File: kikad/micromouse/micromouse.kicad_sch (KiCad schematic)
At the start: 4 parts

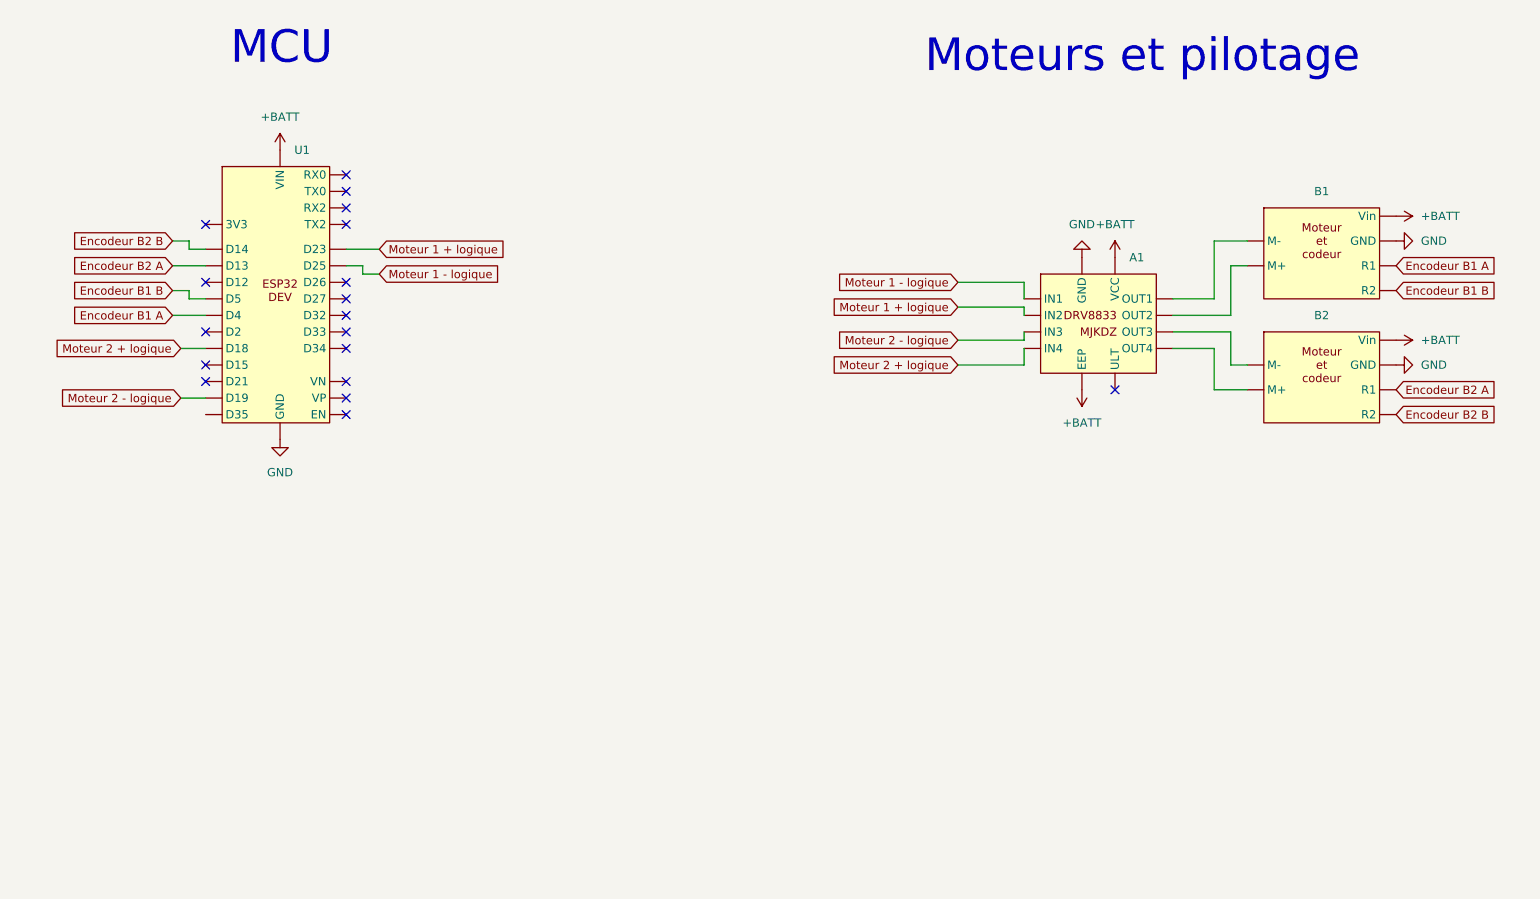
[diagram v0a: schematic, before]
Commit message: Changement micromouse svg
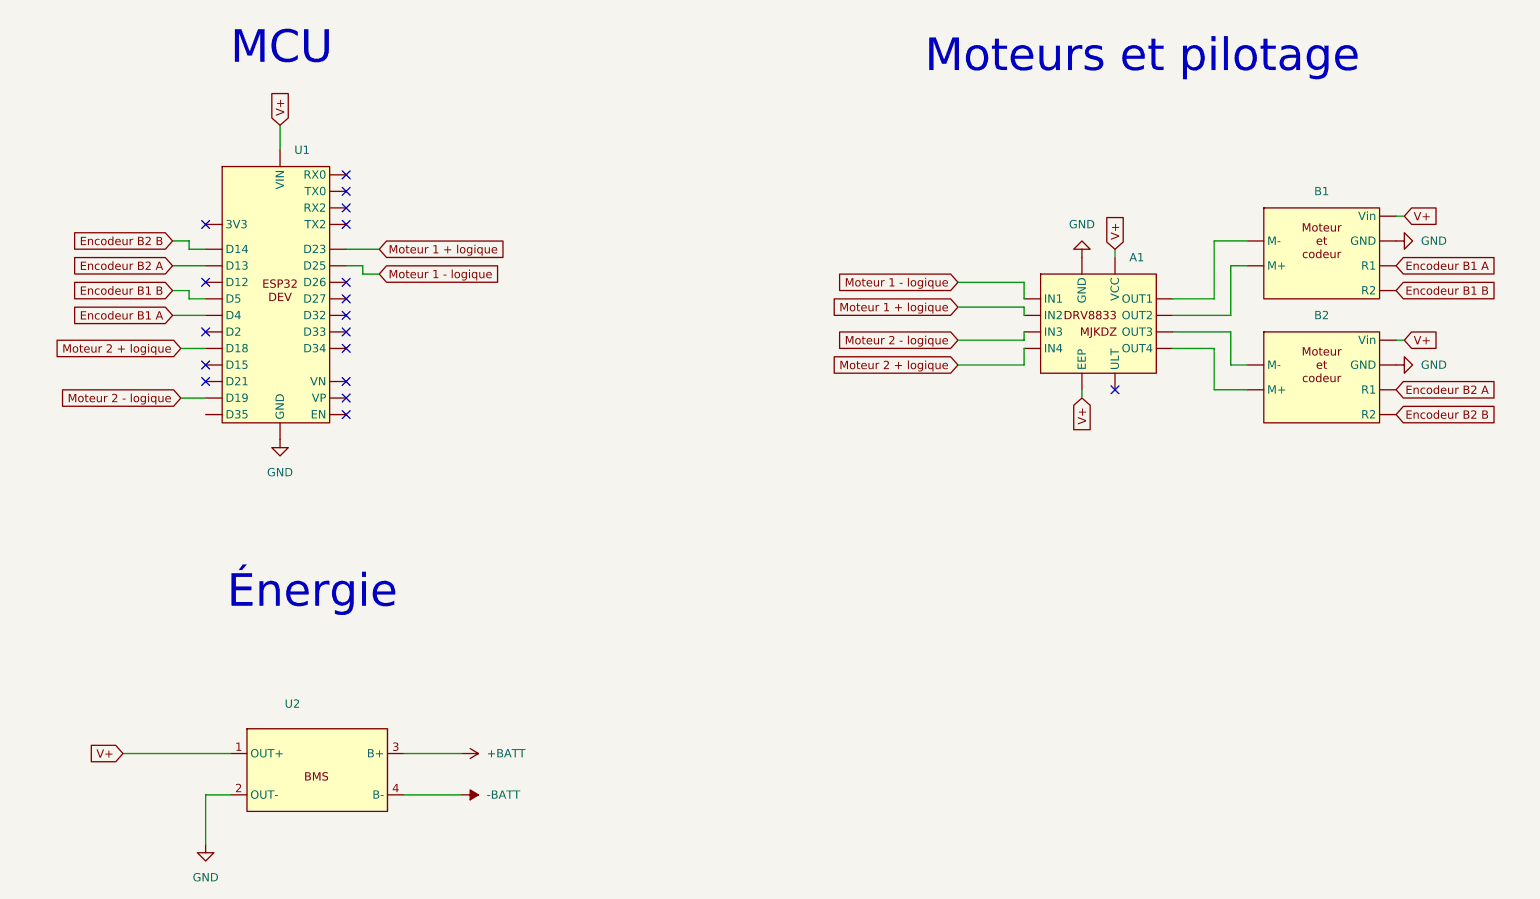
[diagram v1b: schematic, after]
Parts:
- added U2: ~, symbol micromouse:BMS
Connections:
- net +BATT: now also U2.3 (B+); no longer A1. (VCC), B1. (Vin), B2. (Vin), U1. (VP)
- net GND: now also U2.2 (OUT-)
- net V+: now reaches U1. (VP)
- net V+: now also A1. (VCC), B1. (Vin), B2. (Vin), U2.1 (OUT+)
- new net: A1. (VCC), B1. (Vin) (x2)
- new net: A1. (VCC), B2. (Vin) (x2)
- new net -BATT: U2.4 (B-)
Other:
- note added: "Énergie"
